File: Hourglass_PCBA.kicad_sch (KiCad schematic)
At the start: 0 parts

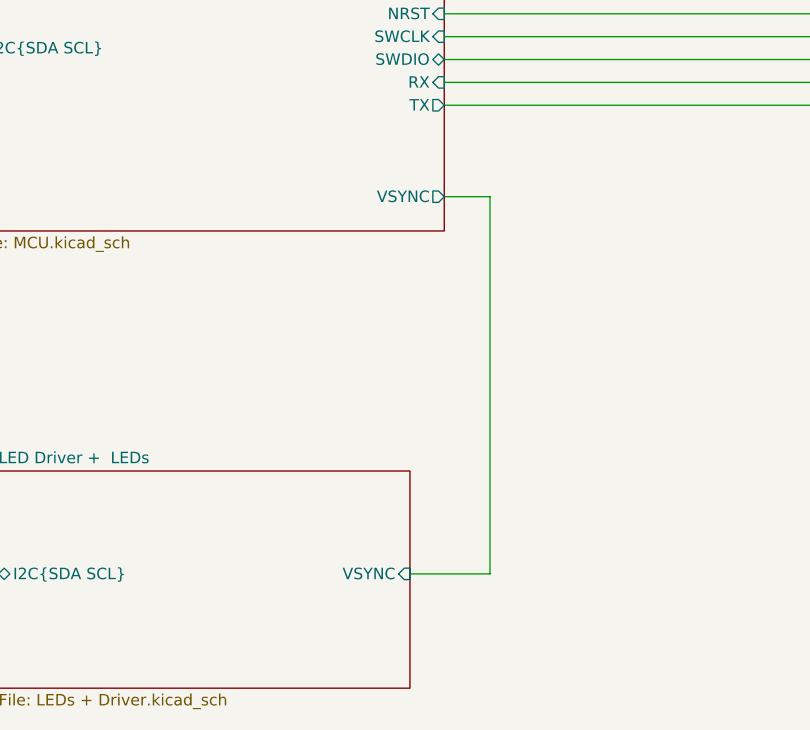
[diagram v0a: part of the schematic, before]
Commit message: Addressed pull-up on NRST. Added GPIO for  VIO_EN. Added comments on schematic and some TPs
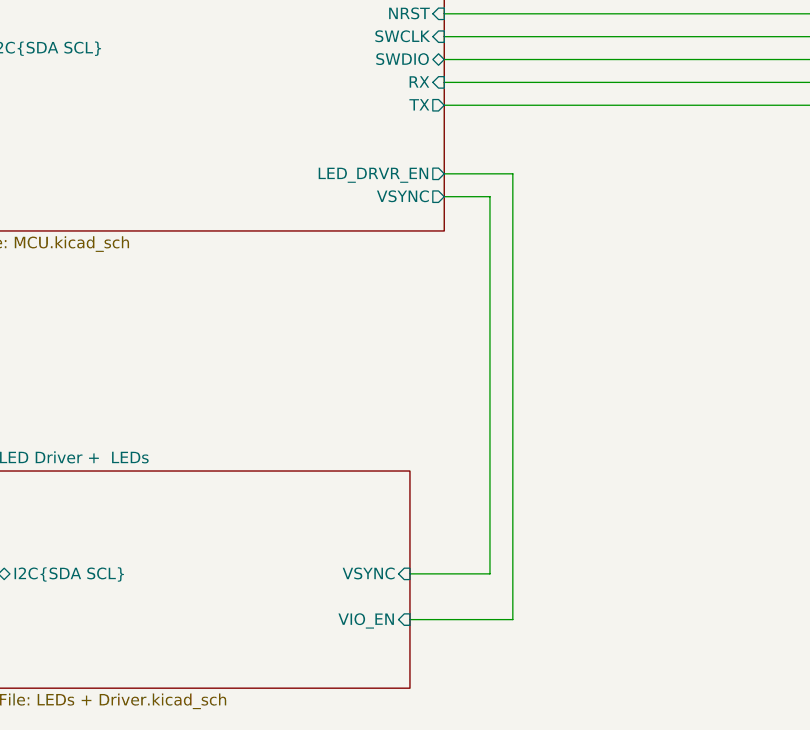
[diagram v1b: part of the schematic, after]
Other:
- sheet LED Driver +  LEDs ports: added VIO_EN; removed none
- sheet MCU ports: added LED_DRVR_EN; removed none
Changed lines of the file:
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@@
 		)
 	)
+	(wire
+		(pts
+			(xy 184.15 147.32) (xy 172.72 147.32)
+		)
+		(stroke
+			(width 0)
+			(type default)
+		)
+	)
 	(bus
 		(pts
@@
 	(wire
 		(pts
+			(xy 176.53 97.79) (xy 184.15 97.79)
+		)
+		(stroke
+			(width 0)
+			(type default)
+		)
+	)
+	(wire
+		(pts
 			(xy 171.45 39.37) (xy 180.34 39.37)
 		)
@@
 	(wire
 		(pts
+			(xy 184.15 97.79) (xy 184.15 147.32)
+		)
+		(stroke
+			(width 0)
+			(type default)
+		)
+	)
+	(wire
+		(pts
 			(xy 181.61 100.33) (xy 181.61 142.24)
 		)
@@
 			"AAAAAAAAAAAAAAAAAAAAAAAAAAAAAAAAAAAAAAAAAAAAAAAAAAAAAAAAAAAAAAAAAAAAAAAAAAAA"
 			"AAAAAAAAAAAAAAAAAAAAAAAAAAAAAAAAAAAAAAAAAAAAAAAAAAAAAAAAAAAAAAAAAAAAAAAAAAAA"
+			"AAAAAAAAAAAAAAAAAAAAAAAAAAAAAAAAAAAAAAAAAAAAAAAAAAAAAAAAAAAAAAAAAAAAAAAAAAAA"
+			"AAAAAAAAAAAAAAAAAAAAAAAAAAAAAAAAAAAAAAAAAAAAAAAAAAAAAAAAAAAAAAAAAAAAAAAAAAAA"
+			"AAAAAAAAAAAAAAAAAAAAAAAAAAAAAAAAAAAAAAAAAAAAAAAAAAAAAAAAAAAAAAAAAAAAAAAAAAAA"
+			"AAAAAAAAAAAAAAAAAAAAAAAAAAAAAAAAAAAAAAAAAAAAAAAAAAAAAAAAAAAAAAAAAAAAAAAAAAAA"
+			"AAAAAAAAAAAAAAAAAAAAAAAAAAAAAAAAAAAAAAAAAAAAAAAAAAAAAAAAAAAAAAAAAAAAAAAAAAAA"
+			"AAAAAAAAAAAAAAAAAAAAAAAAAAAAAAAAAAAAAAAAAAAAAAAAAAAAAAAAAAAAAAAAAAAAAAAAAAAA"
+			"AAAAAAAAAAAAAAAAAAAAAAAAAAAAAAAAAAAAAAAAAAAAAAAAAAAAAAAAAAAAAAAAAAAAAAAAAAAA"
+			"AAAAAAAAAAAAAAAAAAAAAAAAAAAAAAAAAAAAAAAAAAAAAAAAAAAAAAAAAAAAAAAAAAAAAAAAAAAA"
+			"AAAAAAAAAAAAAAAAAAAAAAAAAAAAAAAAAAAAAAAAAAAAAAAAAAAAAAAAAAAAAAAAAAAAAAAAAAAA"
+			"AAAAAAAAAAAAAAAAAAAAAAAAAAAAAAAAAAAAAAAAAAAAAAAAAAAAAAAAAAAAAAAAAAAAAAAAAAAA"
+			"AAAAAAAAAAAAAAAAAAAAAAAAAAAAAAAAAAAAAAAAAAAAAAAAAAAAAAAAAAAAAAAAAAAAAAAAAAAA"
+			"AAAAAAAAAAAAAAAAAAAAAAAAAAAAAAAAAAAAAAAAAAAAAAAAAAAAAAAAAAAAAAAAAAAAAAAAAAAA"
+			"AAAAAAAAAAAAAAAAAAAAAAAAAAAAAAAAAAAAAAAAAAAAAAAAAAAAAAAAAAAAAAAAAAAAAAAAAAAA"
+			"AAAAAAAAAAAAAAAAAAAAAAAAAAAAAAAAAAAAAAAAAAAAAAAAAAAAAAAAAAAAAAAAAAAAAAAAAAAA"
+			"AAAAAAAAAAAAAAAAAAAAAAAAAAAAAAAAAAAAAAAAAAAAAAAAAAAAAAAAAAAAAAAAAAAAAAAAAAAA"
+			"AAAAAAAAAAAAAAAAAAAAAAAAAAAAAAAAAAAAAAAAAAAAAAAAAAAAAAAAAAAAAAAAAAAAAAAAAAAA"
+			"AAAAAAAAAAAAAAAAAAAAAAAAAAAAAAAAAAAAAAAAAAAAAAAAAAAAAAAAAAAAAAAAAAAAAAAAAAAA"
+			"AAAAAAAAAAAAAAAAAAAAAAAAAAAAAAAAAAAAAAAAAAAAAAAAAAAAAAAAAAAAAAAAAAAAAAAAAAAA"
+			"AAAAAAAAAAAAAAAAAAAAAAAAAAAAAAAAAAAAAAAAAAAAAAAAAAAAAAAAAAAAAAAAAAAAAAAAAAAA"
+			"AAAAAAAAAAAAAAAAAAAAAAAAAAAAAAAAAAAAAAAAAAAAAAAAAAAAAAAAAAAAAAAAAAAAAAAAAAAA"
+			"AAAAAAAAAAAAAAAAAAAAAAAAAAAAAAAAAAAAAAAAAAAAAAAAAAAAAAAAAAAAAAAAAAAAAAAAAAAA"
+			"AAAAAAAAAAAAAAAAAAAAAAAAAAAAAAAAAAAAAAAAAAAAAAAAAAAAAAAAAAAAAAAAAAAAAAAAAAAA"
+			"AAAAAAAAAAAAAAAAAAAAAAAAAAAAAAAAAAAAAAAAAAAAAAAAAAAAAAAAAAAAAAAAAAAAAAAAAAAA"
+			"AAAAAAAAAAAAAAAAAAAAAAAAAAAAAAAAAAAAAAAAAAAAAAAAAAAAAAAAAAAAAAAAAAAAAAAAAAAA"
+			"AAAAAAAAAAAAAAAAAAAAAAAAAAAAAAAAAAAAAAAAAAAAAAAAAAAAAAAAAAAAAAAAAAAAAAAAAAAA"
+			"AAAAAAAAAAAAAAAAAAAAAAAAAAAAAAAAAAAAAAAAAAAAAAAAAAAAAAAAAAAAAAAAAAAAAAAAAAAA"
+			"AAAAAAAAAAAAAAAAAAAAAAAAAAAAAAAAAAAAAAAAAAAAAAAAAAAAAAAAAAAAAAAAAAAAAAAAAAAA"
+			"AAAAAAAAAAAAAAAAAAAAAAAAAAAAAAAAAAAAAAAAAAAAAAAAAAAAAAAAAAAAAAAAAAAAAAAAAAAA"
+			"AAAAAAAAAAAAAAAAAAAAAAAAAAAAAAAAAAAAAAAAAAAAAAAAAAAAAAAAAAAAAAAAAAAAAAAAAAAA"
+			"AAAAAAAAAAAAAAAAAAAAAAAAAAAAAAAAAAAAAAAAAAAAAAAAAAAAAAAAAAAAAAAAAAAAAAAAAAAA"
+			"AAAAAAAAAAAAAAAAAAAAAAAAAAAAAAAAAAAAAAAAAAAAAAAAAAAAAAAAAAAAAAAAAAAAAAAAAAAA"
+			"AAAAAAAAAAAAAAAAAAAAAAAAAAAAAAAAAAAAAAAAAAAAAAAAAAAAAAAAAAAAAAAAAAAAAAAAAAAA"
+			"AAAAAAAAAAAAAAAAAAAAAAAAAAAAAAAAAAAAAAAAAAAAAAAAAAAAAAAAAAAAAAAAAAAAAAAAAAAA"
+			"AAAAAAAAAAAAAAAAAAAAAAAAAAAAAAAAAAAAAAAAAAAAAAAAAAAAAAAAAAAAAAAAAAAAAAAAAAAA"
+			"AAAAAAAAAAAAAAAAAAAAAAAAAAAAAAAAAAAAAAAAAAAAAAAAAAAAAAAAAAAAAAAAAAAAAAAAAAAA"
+			"AAAAAAAAAAAAAAAAAAAAAAAAAAAAAAAAAAAAAAAAAAAAAAAAAAAAAAAAAAAAAAAAAAAAAAAAAAAA"
 			"AAAAAAAAAAAAAAAAAAAAAAAAAAAAAAAAAAAAAAAAAA=="
 		)
@@
 			)
 		)
+		(pin "VIO_EN" input
+			(at 172.72 147.32 0)
+			(effects
+				(font
+					(size 1.27 1.27)
+				)
+				(justify right)
+			)
+		)
 		(instances
 			(project "Hourglass_PCBA"
@@
 			(effects
 				(font
+					(size 1.27 1.27)
+				)
+				(justify right)
+			)
+		)
+		(pin "LED_DRVR_EN" output
+			(at 176.53 97.79 0)
+			(effects
+				(font
